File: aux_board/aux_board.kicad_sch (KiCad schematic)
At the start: 17 parts, among them J1 Conn_01x02_Pin, J2 Conn_02x01, J3 Conn_02x01, J4 Conn_02x13_Odd_Even, J5 Conn_02x04_Odd_Even

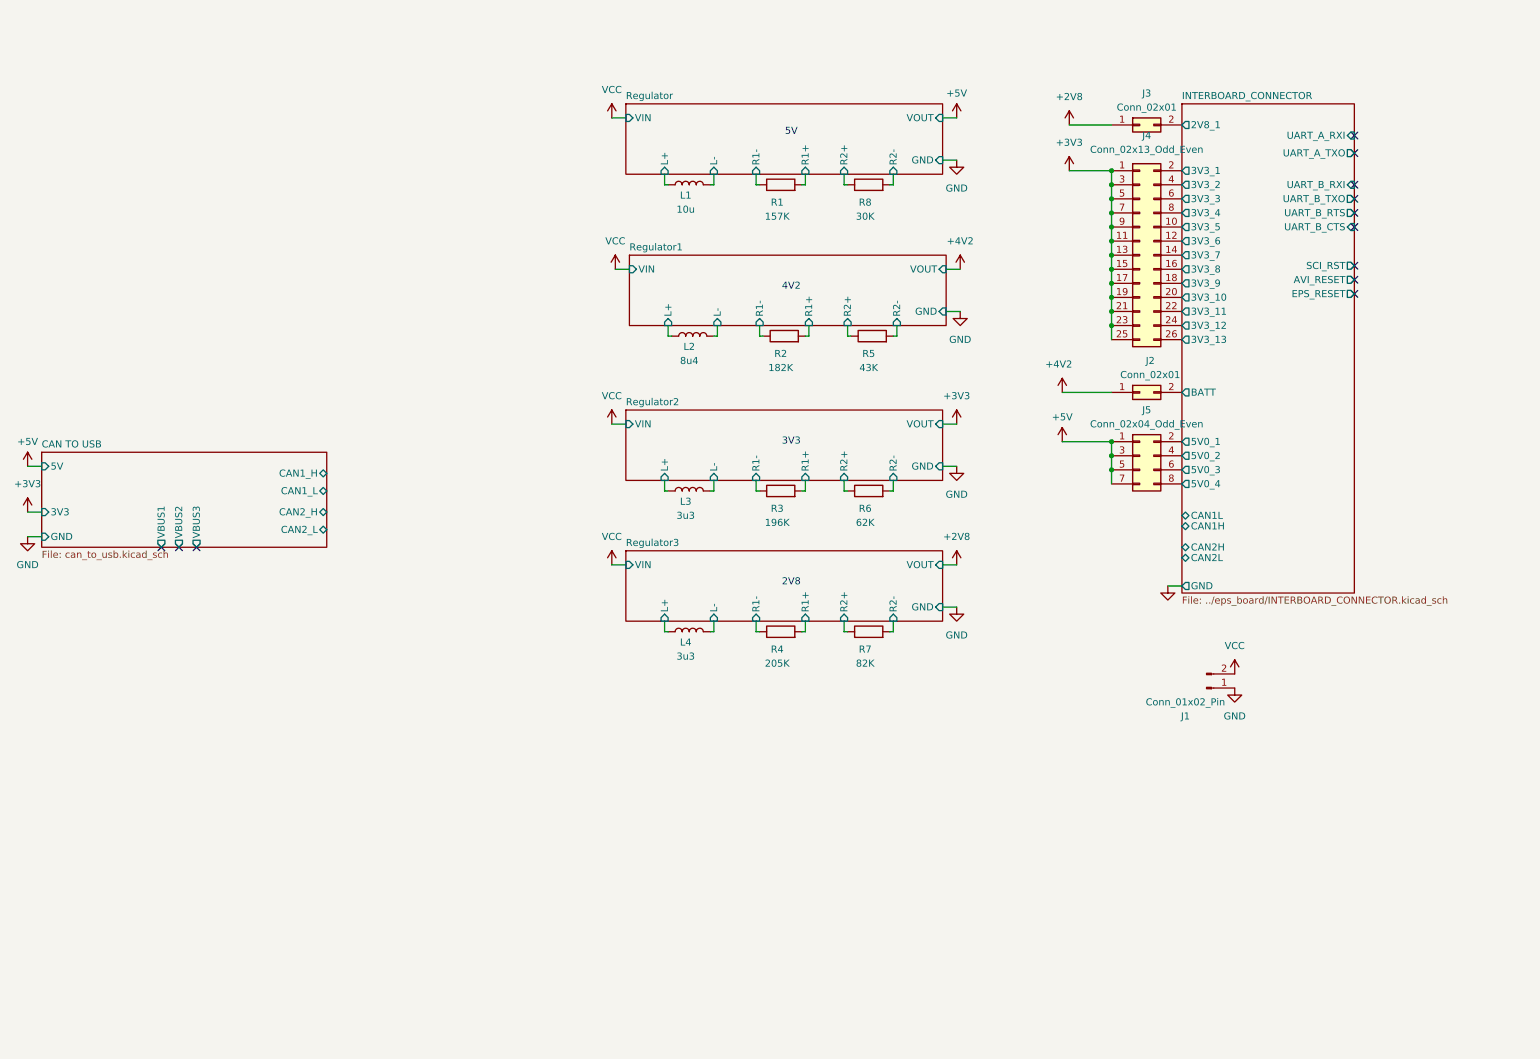
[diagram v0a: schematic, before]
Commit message: aux board: use active FTI chip FT230X that has all the functionality needed TX RX RTS CTS
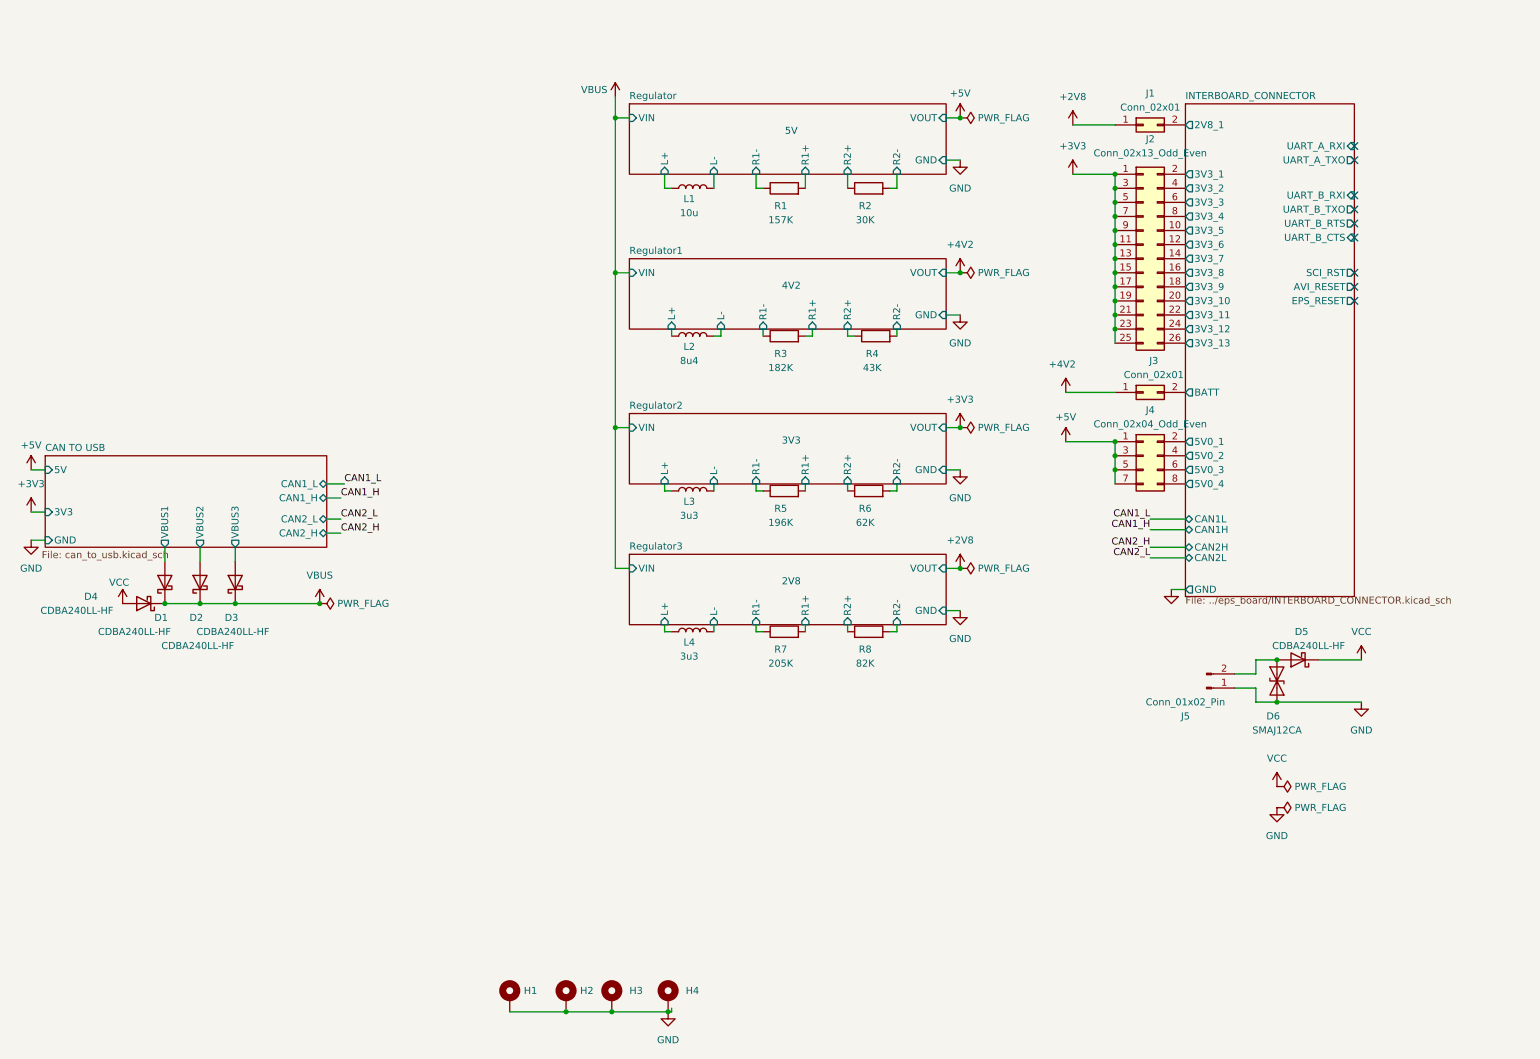
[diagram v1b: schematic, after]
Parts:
- added D1, D2, D3, D4, D5: CDBA240LL-HF, Diode_SMD:D_SMA_Handsoldering, symbol Device:D_Schottky
- added D6: SMAJ12CA, Diode_SMD:D_SMA, symbol Diode:SMAJ12CA
- added H1, H2, H3, H4: MountingHole_Pad, Project:MountingHole_4.3mm_M4_Pad_Via_Custom, symbol Mechanical:MountingHole_Pad
- J1: renamed from J3; footprint (none) -> Connector_PinHeader_2.54mm:PinHeader_1x02_P2.54mm_Vertical
- J2: renamed from J4; footprint (none) -> Connector_PinHeader_2.54mm:PinHeader_2x13_P2.54mm_Vertical
- J3: renamed from J2; footprint (none) -> Connector_PinHeader_2.54mm:PinHeader_2x01_P2.54mm_Vertical
- J4: renamed from J5; footprint (none) -> Connector_PinHeader_2.54mm:PinHeader_2x04_P2.54mm_Vertical
- J5: renamed from J1; footprint (none) -> Connector_PinHeader_2.54mm:PinHeader_1x02_P2.54mm_Vertical
- L1: footprint (none) -> Capacitor_SMD:C_0805_2012Metric_Pad1.18x1.45mm_HandSolder
- L2, L3, L4: footprint (none) -> Inductor_SMD:L_1210_3225Metric_Pad1.42x2.65mm_HandSolder
- R1, R6: footprint (none) -> Resistor_SMD:R_0603_1608Metric_Pad0.98x0.95mm_HandSolder
- R2: renamed from R8; footprint (none) -> Resistor_SMD:R_0603_1608Metric_Pad0.98x0.95mm_HandSolder
- R3: renamed from R2; footprint (none) -> Resistor_SMD:R_0603_1608Metric_Pad0.98x0.95mm_HandSolder
- R4: renamed from R5; footprint (none) -> Resistor_SMD:R_0603_1608Metric_Pad0.98x0.95mm_HandSolder
- R5: renamed from R3; footprint (none) -> Resistor_SMD:R_0603_1608Metric_Pad0.98x0.95mm_HandSolder
- R7: renamed from R4; footprint (none) -> Resistor_SMD:R_0603_1608Metric_Pad0.98x0.95mm_HandSolder
- R8: renamed from R7; footprint (none) -> Resistor_SMD:R_0603_1608Metric_Pad0.98x0.95mm_HandSolder
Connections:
- net CAN TO USB/VBUS1: now also D1.2 (A)
- net CAN TO USB/VBUS2: now also D2.2 (A)
- net CAN TO USB/VBUS3: now also D3.2 (A)
- net GND: now also D6.1 (A1), H1.1, H2.1, H3.1, H4.1
- net VCC: now also D4.2 (A), D5.1 (K); no longer J5.2 (Pin_2)
- new net: D5.2 (A), D6.2 (A2), J5.2 (Pin_2)
- new net VBUS: D1.1 (K), D2.1 (K), D3.1 (K), D4.1 (K)
- no-connect marks 12 -> 9
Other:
- moved on the sheet: J1, J2, J3, J4, L1, L3, L4, R1, R2, R4, R5, R7

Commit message: replace nearly all buck converters with boost buck (missing is 5raw
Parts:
- removed J1: Conn_02x01, Connector_PinHeader_2.54mm:PinHeader_1x02_P2.54mm_Vertical, symbol Connector_Generic:Conn_02x01
- removed L4: 3u3, Inductor_SMD:L_1210_3225Metric_Pad1.42x2.65mm_HandSolder, symbol Device:L
- removed R4: 43K, Resistor_SMD:R_0603_1608Metric_Pad0.98x0.95mm_HandSolder, symbol Device:R
- removed R5: 196K, Resistor_SMD:R_0603_1608Metric_Pad0.98x0.95mm_HandSolder, symbol Device:R
- removed R6: 62K, Resistor_SMD:R_0603_1608Metric_Pad0.98x0.95mm_HandSolder, symbol Device:R
- removed R7: 205K, Resistor_SMD:R_0603_1608Metric_Pad0.98x0.95mm_HandSolder, symbol Device:R
- removed R8: 82K, Resistor_SMD:R_0603_1608Metric_Pad0.98x0.95mm_HandSolder, symbol Device:R
- L1: value 10u -> 1u; footprint Capacitor_SMD:C_0805_2012Metric_Pad1.18x1.45mm_HandSolder -> Inductor_SMD:L_1008_2520Metric_Pad1.43x2.20mm_HandSolder
- L2: value 8u4 -> 1u; footprint Inductor_SMD:L_1210_3225Metric_Pad1.42x2.65mm_HandSolder -> Inductor_SMD:L_1008_2520Metric_Pad1.43x2.20mm_HandSolder
- L3: value 3u3 -> 1u; footprint Inductor_SMD:L_1210_3225Metric_Pad1.42x2.65mm_HandSolder -> Inductor_SMD:L_1008_2520Metric_Pad1.43x2.20mm_HandSolder
- R1: value 157K -> 806K
- R2: value 30K -> 673K4
- R3: value 182K -> 511K
- renumbered D5 to D1, D6 to D2, D1 to D3, D2 to D4, D3 to D5, D4 to D6, J2 to J1, J3 to J2, J4 to J3, J5 to J4
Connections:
- net +4V2 renamed +VBAT
- net Regulator/L+ renamed Regulator 5V/LX1
- net Regulator/L- renamed Regulator 5V/LX2
- net Regulator/R1+ renamed Regulator 5V/R+
- net Regulator/R1- renamed Regulator 5V/R-
- net Regulator/R2+ renamed Regulator 4V2/R-
- net Regulator/R2- renamed Regulator 4V2/R+
- net Regulator1/L+ renamed Regulator 4V2/LX1
- net Regulator1/L- renamed Regulator 4V2/LX2
- net Regulator1/R1+ renamed Regulator 3V3/R+
- net Regulator1/R1- renamed Regulator 3V3/R-
- net Regulator2/L+ renamed Regulator 3V3/LX1
- net Regulator2/L- renamed Regulator 3V3/LX2
- no-connect marks 9 -> 10
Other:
- removed sheet Regulator
- removed sheet Regulator1
- removed sheet Regulator2
- removed sheet Regulator3
- added sheet Regulator 3V3 (../sci_board/power_regulator_mp3416.kicad_sch)
- added sheet Regulator 4V2 (../sci_board/power_regulator_mp3416.kicad_sch)
- added sheet Regulator 5V (../sci_board/power_regulator_mp3416.kicad_sch)
- note removed: "2V8"
- note removed: "3V3"
- note removed: "4V2"
- note removed: "5V"
- moved on the sheet: D3, D4, D5, D6

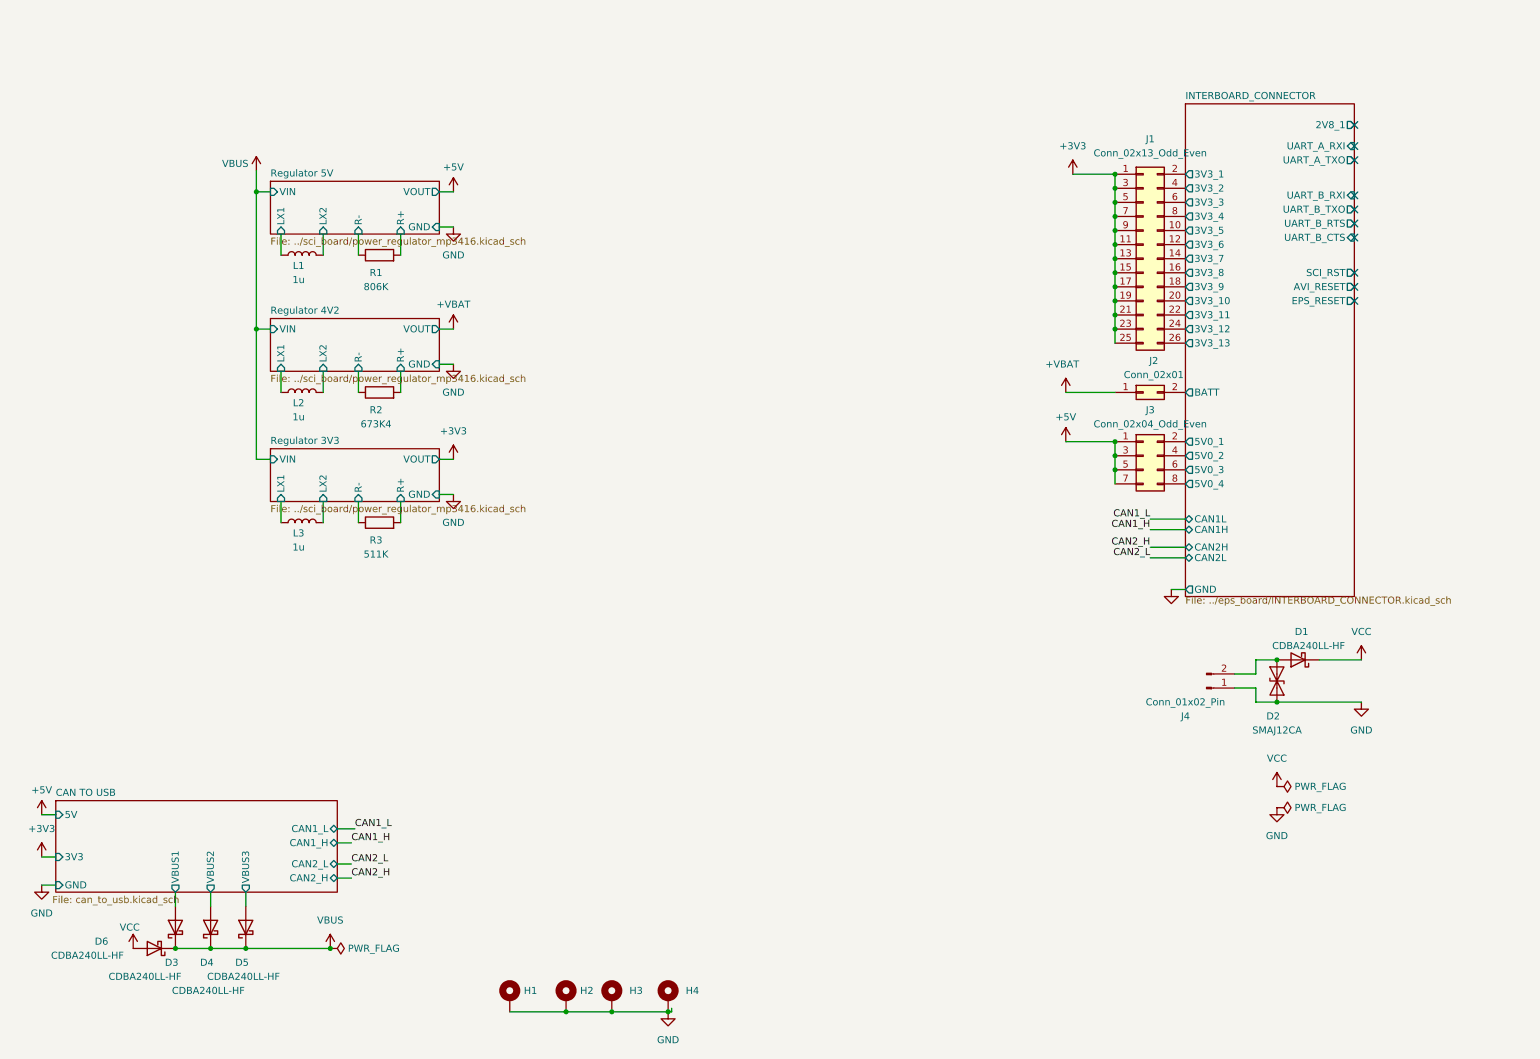
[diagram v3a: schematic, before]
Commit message: AUX to PCI104
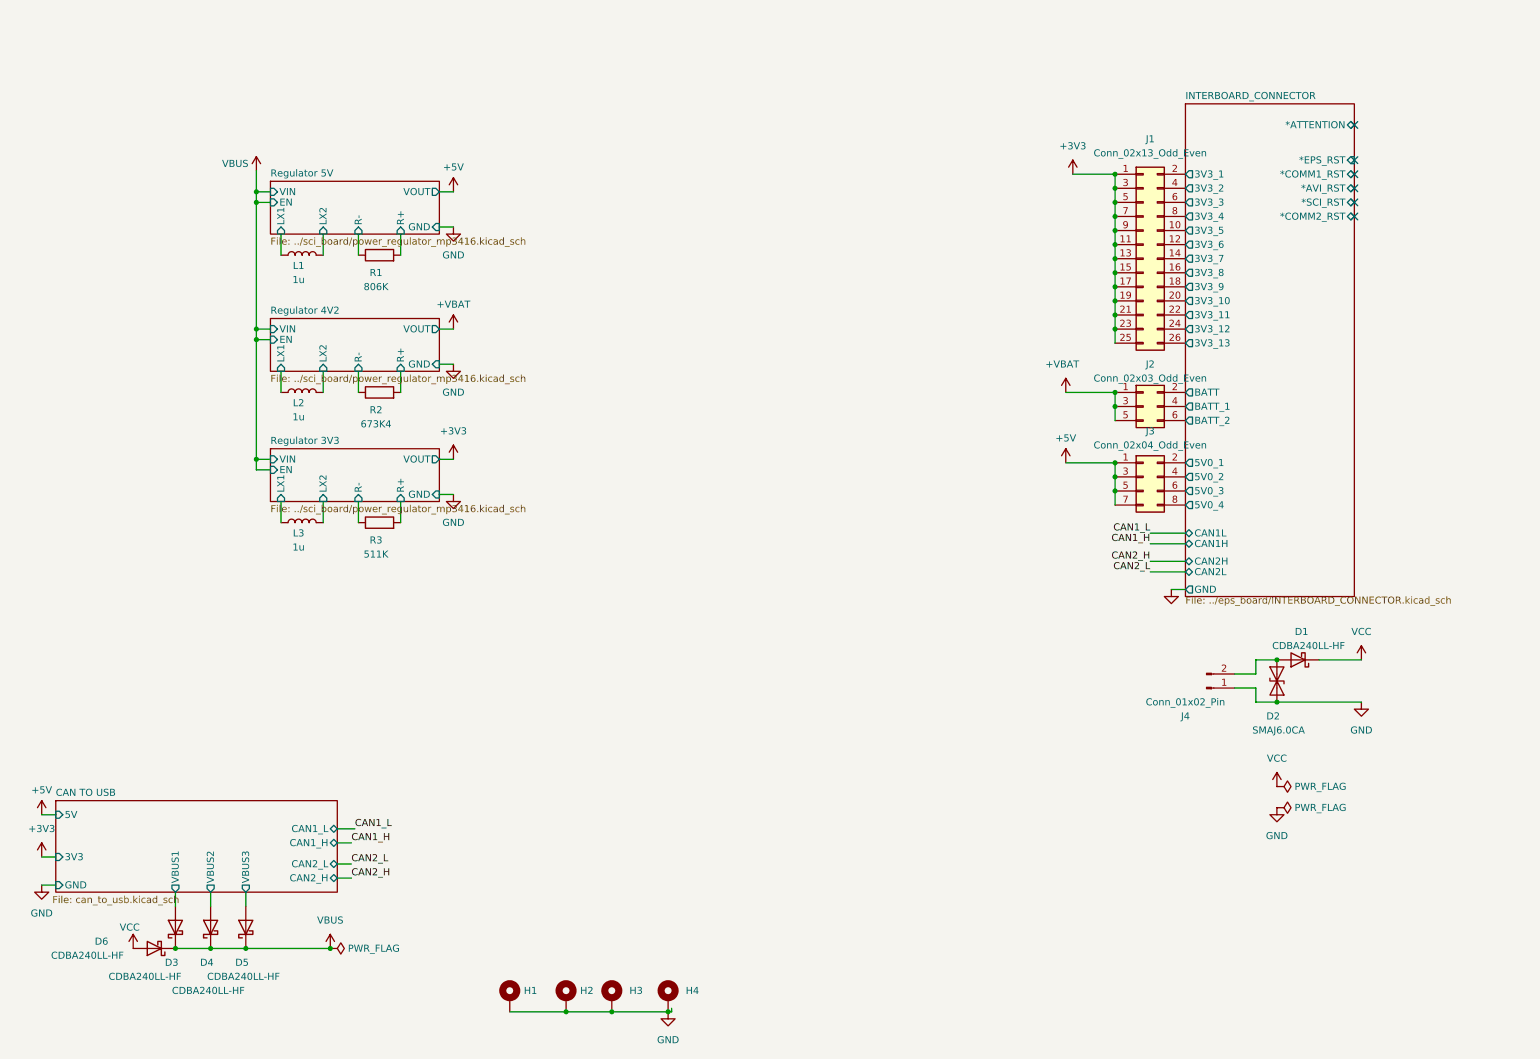
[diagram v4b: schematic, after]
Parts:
- removed J2: Conn_02x01, Connector_PinHeader_2.54mm:PinHeader_2x01_P2.54mm_Vertical, symbol Connector_Generic:Conn_02x01
- added J2: Conn_02x03_Odd_Even, Connector_PinHeader_2.54mm:PinHeader_2x03_P2.54mm_Vertical, symbol Connector_Generic:Conn_02x03_Odd_Even
- D2: value SMAJ12CA -> SMAJ6.0CA; footprint Diode_SMD:D_SMA -> Diode_SMD:D_SMA_Handsoldering
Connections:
- net +VBAT: now also J2.1 (Pin_1), J2.3 (Pin_3), J2.5 (Pin_5)
- net INTERBOARD_CONNECTOR/BATT: now also J2.2 (Pin_2)
- new net INTERBOARD_CONNECTOR/BATT_1: J2.4 (Pin_4)
- new net INTERBOARD_CONNECTOR/BATT_2: J2.6 (Pin_6)
- no-connect marks 10 -> 6
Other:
- sheet INTERBOARD_CONNECTOR ports: added *ATTENTION, *AVI_RST, *COMM1_RST, *COMM2_RST, *EPS_RST, *SCI_RST, BATT_1, BATT_2; removed 2V8_1, AVI_RESET, EPS_RESET, SCI_RST, UART_A_RXI, UART_A_TXO, UART_B_CTS, UART_B_RTS, UART_B_RXI, UART_B_TXO
- sheet Regulator 3V3 ports: added EN; removed none
- sheet Regulator 4V2 ports: added EN; removed none
- sheet Regulator 5V ports: added EN; removed none
- moved on the sheet: J3
